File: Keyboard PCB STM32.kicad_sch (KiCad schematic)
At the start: 18 parts, among them J1 USB_C_Receptacle_USB2.0_14P, SW68 SW_Push, U1 XC6206PxxxMR, U2 SRV05-4, U3 STM32F072CBTx

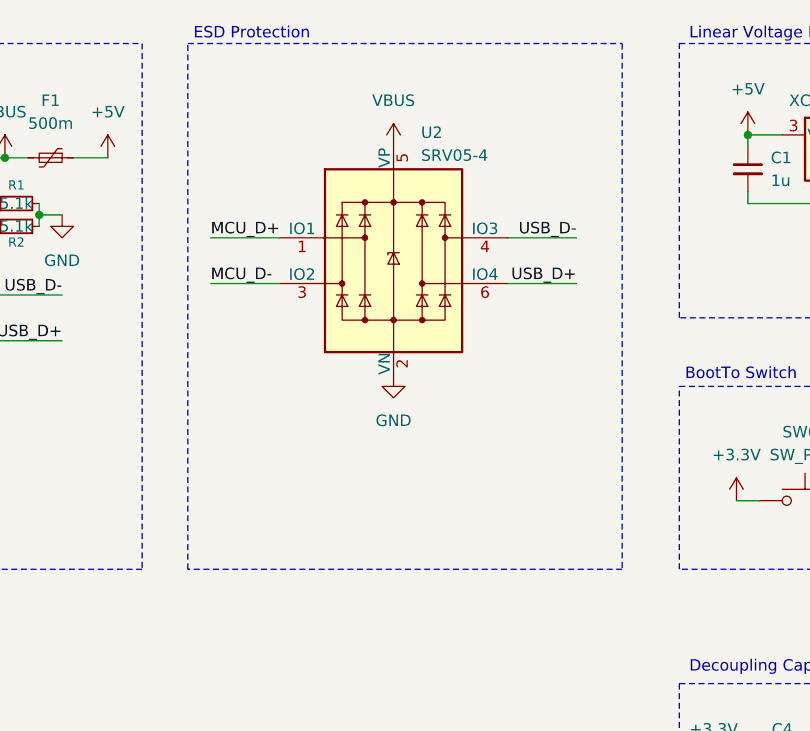
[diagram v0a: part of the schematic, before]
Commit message: Update to ESD protection
Changed ESD from SRV05-4 to USBLC6-2SC6
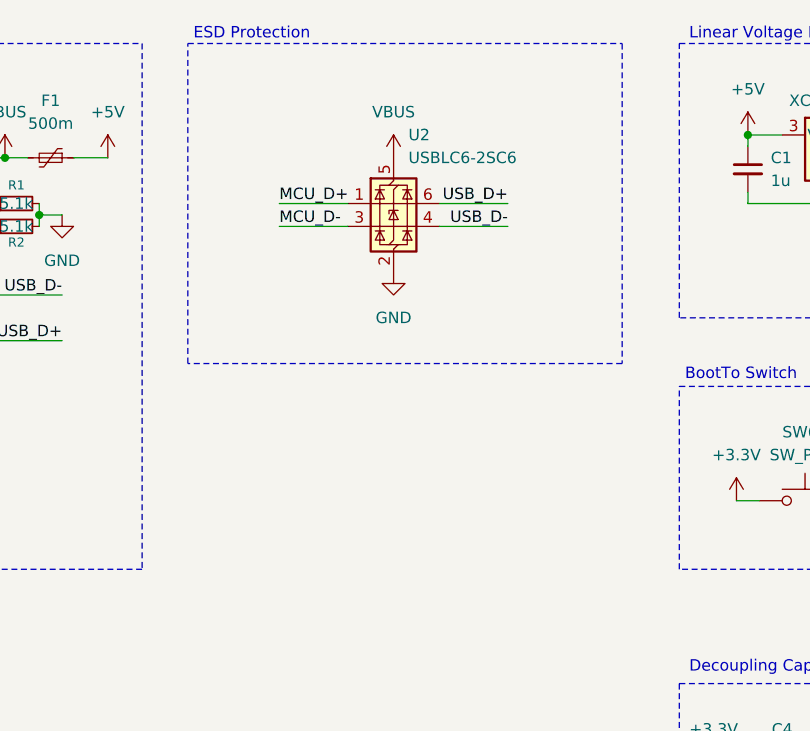
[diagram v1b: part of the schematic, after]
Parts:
- removed U2: SRV05-4, Package_TO_SOT_SMD:SOT-23-6, symbol Power_Protection:SRV05-4
- added U2: USBLC6-2SC6, Package_TO_SOT_SMD:SOT-23-6, symbol Power_Protection:USBLC6-2SC6
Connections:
- net GND: now also U2.2 (GND)
- net MCU_D+: now also U2.1 (I/O1)
- net MCU_D-: now also U2.3 (I/O2)
- net USB_D+: now also U2.6 (I/O1)
- net USB_D-: now also U2.4 (I/O2)
- net VBUS: now also U2.5 (VBUS)
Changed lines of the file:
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@@
 	(rectangle
 		(start 78.74 27.94)
-		(end 127 86.36)
+		(end 127 63.5)
 		(stroke
 			(width 0)
@@
 	(wire
 		(pts
-			(xy 81.28 49.53) (xy 88.9 49.53)
+			(xy 54.61 55.88) (xy 55.88 55.88)
 		)
 		(stroke
@@
 	(wire
 		(pts
-			(xy 54.61 55.88) (xy 55.88 55.88)
+			(xy 160.02 38.1) (xy 162.56 38.1)
 		)
 		(stroke
@@
 	(wire
 		(pts
-			(xy 160.02 38.1) (xy 162.56 38.1)
+			(xy 62.23 46.99) (xy 62.23 48.26)
 		)
 		(stroke
@@
 	(wire
 		(pts
-			(xy 62.23 46.99) (xy 62.23 48.26)
+			(xy 140.97 38.1) (xy 140.97 39.37)
 		)
 		(stroke
@@
 	(wire
 		(pts
-			(xy 140.97 38.1) (xy 140.97 39.37)
+			(xy 162.56 38.1) (xy 162.56 39.37)
 		)
 		(stroke
@@
 	(wire
 		(pts
-			(xy 162.56 38.1) (xy 162.56 39.37)
+			(xy 217.17 38.1) (xy 219.71 38.1)
 		)
 		(stroke
@@
 	(wire
 		(pts
-			(xy 217.17 38.1) (xy 219.71 38.1)
+			(xy 88.9 48.26) (xy 96.52 48.26)
 		)
 		(stroke
@@
 	(wire
 		(pts
-			(xy 114.3 49.53) (xy 121.92 49.53)
+			(xy 165.1 78.74) (xy 167.64 78.74)
 		)
 		(stroke
@@
 	(wire
 		(pts
-			(xy 81.28 54.61) (xy 88.9 54.61)
+			(xy 162.56 45.72) (xy 162.56 44.45)
 		)
 		(stroke
@@
 	(wire
 		(pts
-			(xy 165.1 78.74) (xy 167.64 78.74)
+			(xy 154.94 109.22) (xy 149.86 109.22)
 		)
 		(stroke
@@
 	(wire
 		(pts
-			(xy 162.56 45.72) (xy 162.56 44.45)
+			(xy 152.4 78.74) (xy 157.48 78.74)
 		)
 		(stroke
@@
 	(wire
 		(pts
-			(xy 154.94 109.22) (xy 149.86 109.22)
+			(xy 31.75 78.74) (xy 39.37 78.74)
 		)
 		(stroke
@@
 	(wire
 		(pts
-			(xy 152.4 78.74) (xy 157.48 78.74)
+			(xy 55.88 53.34) (xy 55.88 55.88)
 		)
 		(stroke
@@
 	(wire
 		(pts
-			(xy 31.75 78.74) (xy 39.37 78.74)
+			(xy 88.9 45.72) (xy 96.52 45.72)
 		)
 		(stroke
@@
 	(wire
 		(pts
-			(xy 55.88 53.34) (xy 55.88 55.88)
+			(xy 62.23 46.99) (xy 64.77 46.99)
 		)
 		(stroke
@@
 	(wire
 		(pts
-			(xy 62.23 46.99) (xy 64.77 46.99)
+			(xy 66.04 40.64) (xy 69.85 40.64)
 		)
 		(stroke
@@
 	(wire
 		(pts
-			(xy 114.3 54.61) (xy 121.92 54.61)
+			(xy 106.68 48.26) (xy 114.3 48.26)
 		)
 		(stroke
@@
 	(wire
 		(pts
-			(xy 66.04 40.64) (xy 69.85 40.64)
+			(xy 165.1 109.22) (xy 170.18 109.22)
 		)
 		(stroke
@@
 	(wire
 		(pts
-			(xy 165.1 109.22) (xy 170.18 109.22)
+			(xy 154.94 114.3) (xy 160.02 114.3)
 		)
 		(stroke
@@
 	(wire
 		(pts
-			(xy 154.94 114.3) (xy 160.02 114.3)
+			(xy 64.77 55.88) (xy 55.88 55.88)
 		)
 		(stroke
@@
 	(wire
 		(pts
-			(xy 64.77 55.88) (xy 55.88 55.88)
+			(xy 106.68 45.72) (xy 114.3 45.72)
 		)
 		(stroke
@@
 	)
 	(label "USB_D+"
-		(at 121.92 54.61 180)
+		(at 114.3 45.72 180)
 		(effects
 			(font
@@
 	)
 	(label "MCU_D-"
-		(at 81.28 54.61 0)
+		(at 88.9 48.26 0)
 		(effects
 			(font
@@
 	)
 	(label "USB_D-"
-		(at 121.92 49.53 180)
+		(at 114.3 48.26 180)
 		(effects
 			(font
@@
 	)
 	(label "MCU_D+"
-		(at 81.28 49.53 0)
+		(at 88.9 45.72 0)
 		(effects
 			(font
@@
 	(symbol
 		(lib_id "power:GND")
-		(at 101.6 64.77 0)
+		(at 101.6 53.34 0)
 		(unit 1)
 		(exclude_from_sim no)
@@
 		(fields_autoplaced yes)
 		(property "Reference" "#PWR06"
-			(at 101.6 71.12 0)
+			(at 101.6 59.69 0)
 			(effects
 				(font
@@
 		)
 		(property "Value" "GND"
-			(at 101.6 69.85 0)
+			(at 101.6 58.42 0)
 			(effects
 				(font
@@
 		)
 		(property "Footprint" ""
-			(at 101.6 64.77 0)
+			(at 101.6 53.34 0)
 			(effects
 				(font
@@
 		)
 		(property "Datasheet" ""
-			(at 101.6 64.77 0)
+			(at 101.6 53.34 0)
 			(effects
 				(font
@@
 		)
 		(property "Description" "Power symbol creates a global label with name \"GND\" , ground"
-			(at 101.6 64.77 0)
+			(at 101.6 53.34 0)
 			(effects
 				(font
@@
 		)
 		(instances
-			(project ""
+			(project "Keyboard PCB STM32"
 				(path "/d7b46417-6e9b-40e7-895f-68f7a27257b4"
 					(reference "#PWR06")
@@
 	)
 	(symbol
+		(lib_id "Power_Protection:USBLC6-2SC6")
+		(at 101.6 45.72 0)
+		(unit 1)
+		(exclude_from_sim no)
+		(in_bom yes)
+		(on_board yes)
+		(dnp no)
+		(fields_autoplaced yes)
+		(property "Reference" "U2"
+			(at 103.2511 38.1 0)
+			(effects
+				(font
+					(size 1.27 1.27)
+				)
+				(justify left)
+			)
+		)
+		(property "Value" "USBLC6-2SC6"
+			(at 103.2511 40.64 0)
+			(effects
+				(font
+					(size 1.27 1.27)
+				)
+				(justify left)
+			)
+		)
+		(property "Footprint" "Package_TO_SOT_SMD:SOT-23-6"
+			(at 102.87 52.07 0)
+			(effects
+				(font
+					(size 1.27 1.27)
+					(italic yes)
+				)
+				(justify left)
+				(hide yes)
+			)
+		)
+		(property "Datasheet" "https://www.st.com/resource/en/datasheet/usblc6-2.pdf"
+			(at 102.87 53.975 0)
+			(effects
+				(font
+					(size 1.27 1.27)
+				)
+				(justify left)
+				(hide yes)
+			)
+		)
+		(property "Description" "Very low capacitance ESD protection diode, 2 data-line, SOT-23-6"
+			(at 101.6 45.72 0)
+			(effects
+				(font
+					(size 1.27 1.27)
+				)
+				(hide yes)
+			)
+		)
+		(pin "4"
+		)
+		(pin "1"
+		)
+		(pin "2"
+		)
+		(pin "6"
+		)
+		(pin "3"
+		)
+		(pin "5"
+		)
+		(instances
+			(project ""
+				(path "/d7b46417-6e9b-40e7-895f-68f7a27257b4"
+					(reference "U2")
+					(unit 1)
+				)
+			)
+		)
+	)
+	(symbol
 		(lib_id "Device:C_Small")
 		(at 140.97 41.91 0)
@@
 	(symbol
 		(lib_id "power:VBUS")
-		(at 101.6 39.37 0)
+		(at 101.6 40.64 0)
 		(unit 1)
 		(exclude_from_sim no)
@@
 		(fields_autoplaced yes)
 		(property "Reference" "#PWR013"
-			(at 101.6 43.18 0)
+			(at 101.6 44.45 0)
 			(effects
 				(font
@@
 		)
 		(property "Value" "VBUS"
-			(at 101.6 34.29 0)
+			(at 101.6 35.56 0)
 			(effects
 				(font
@@
 		)
 		(property "Footprint" ""
-			(at 101.6 39.37 0)
+			(at 101.6 40.64 0)
 			(effects
 				(font
@@
 		)
 		(property "Datasheet" ""
-			(at 101.6 39.37 0)
+			(at 101.6 40.64 0)
 			(effects
 				(font
@@
 		)
 		(property "Description" "Power symbol creates a global label with name \"VBUS\""
-			(at 101.6 39.37 0)
+			(at 101.6 40.64 0)
 			(effects
 				(font
@@
 		)
 		(instances
-			(project ""
+			(project "Keyboard PCB STM32"
 				(path "/d7b46417-6e9b-40e7-895f-68f7a27257b4"
 					(reference "#PWR013")
@@
 					(unit 1)
 				)
-			)
-		)
-	)
-	(symbol
-		(lib_id "Power_Protection:SRV05-4")
-		(at 101.6 52.07 0)
-		(unit 1)
-		(exclude_from_sim no)
-		(in_bom yes)
-		(on_board yes)
-		(dnp no)
-		(property "Reference" "U2"
-			(at 104.648 37.846 0)
-			(effects
-				(font
-					(size 1.27 1.27)
-				)
-				(justify left)
-			)
-		)
-		(property "Value" "SRV05-4"
-			(at 104.648 40.386 0)
-			(effects
-				(font
-					(size 1.27 1.27)
-				)
-				(justify left)
-			)
-		)
-		(property "Footprint" "Package_TO_SOT_SMD:SOT-23-6"
-			(at 119.38 63.5 0)
-			(effects
-				(font
-					(size 1.27 1.27)
-				)
-				(hide yes)
-			)
-		)
-		(property "Datasheet" "http://www.onsemi.com/pub/Collateral/SRV05-4-D.PDF"
-			(at 101.6 52.07 0)
-			(effects
-				(font
-					(size 1.27 1.27)
-				)
-				(hide yes)
-			)
-		)
-		(property "Description" "ESD Protection Diodes with Low Clamping Voltage, SOT-23-6"
-			(at 101.6 52.07 0)
-			(effects
-				(font
-					(size 1.27 1.27)
-				)
-				(hide yes)
-			)
-		)
-		(pin "2"
-		)
-		(pin "6"
-		)
-		(pin "1"
-		)
-		(pin "4"
-		)
-		(pin "3"
-		)
-		(pin "5"
-		)
-		(instances
-			(project ""
-				(path "/d7b46417-6e9b-40e7-895f-68f7a27257b4"
-					(reference "U2")
-					(unit 1)
-				)

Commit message: Add files via upload
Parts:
- added SW69: SW_Push, Button_Switch_SMD:SW_Push_1P1T_XKB_TS-1187A, symbol Switch:SW_Push
- SW68: footprint Button_Switch_SMD:SW_SPST_TS-1088-xR020 -> Button_Switch_SMD:Panasonic_EVQPUL_EVQPUC
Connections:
- net +3.3V: now also SW69.1
- net BOOT: now also SW69.2
- no-connect marks 14 -> 15
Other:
- moved on the sheet: R3, SW68
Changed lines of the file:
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@@
 	)
 	(rectangle
-		(start 133.35 66.04)
-		(end 172.72 86.36)
+		(start 133.35 63.5)
+		(end 172.72 90.17)
 		(stroke
 			(width 0)
@@
 	(text "BootTo Switch"
 		(exclude_from_sim no)
-		(at 140.208 64.77 0)
+		(at 140.208 62.23 0)
 		(effects
 			(font
@@
 	)
 	(junction
+		(at 152.4 73.66)
+		(diameter 0)
+		(color 0 0 0 0)
+	)
+	(junction
 		(at 219.71 38.1)
 		(diameter 0)
@@
 	)
 	(junction
+		(at 142.24 73.66)
+		(diameter 0)
+		(color 0 0 0 0)
+	)
+	(junction
 		(at 154.94 109.22)
 		(diameter 0)
@@
 	)
 	(no_connect
+		(at 240.03 50.8)
+	)
+	(no_connect
 		(at 204.47 96.52)
 	)
@@
 	(wire
 		(pts
+			(xy 152.4 73.66) (xy 152.4 85.09)
+		)
+		(stroke
+			(width 0)
+			(type default)
+		)
+	)
+	(wire
+		(pts
 			(xy 54.61 55.88) (xy 55.88 55.88)
 		)
@@
 	(wire
 		(pts
+			(xy 142.24 73.66) (xy 142.24 85.09)
+		)
+		(stroke
+			(width 0)
+			(type default)
+		)
+	)
+	(wire
+		(pts
 			(xy 88.9 48.26) (xy 96.52 48.26)
 		)
@@
 	(wire
 		(pts
-			(xy 165.1 78.74) (xy 167.64 78.74)
+			(xy 162.56 45.72) (xy 162.56 44.45)
 		)
 		(stroke
@@
 	(wire
 		(pts
-			(xy 162.56 45.72) (xy 162.56 44.45)
+			(xy 154.94 109.22) (xy 149.86 109.22)
 		)
 		(stroke
@@
 	(wire
 		(pts
-			(xy 154.94 109.22) (xy 149.86 109.22)
+			(xy 152.4 73.66) (xy 157.48 73.66)
 		)
 		(stroke
@@
 	(wire
 		(pts
-			(xy 152.4 78.74) (xy 157.48 78.74)
+			(xy 31.75 78.74) (xy 39.37 78.74)
 		)
 		(stroke
@@
 	(wire
 		(pts
-			(xy 31.75 78.74) (xy 39.37 78.74)
+			(xy 167.64 73.66) (xy 165.1 73.66)
 		)
 		(stroke
@@
 	(wire
 		(pts
-			(xy 139.7 78.74) (xy 142.24 78.74)
+			(xy 139.7 73.66) (xy 142.24 73.66)
 		)
 		(stroke
@@
 		)
 	)
-	(global_label "BOOT"
-		(shape input)
-		(at 154.94 78.74 90)
-		(fields_autoplaced yes)
-		(effects
-			(font
-				(size 1.27 1.27)
-			)
-			(justify left)
-		)
-		(property "Intersheetrefs" "${INTERSHEET_REFS}"
-			(at 154.94 70.8562 90)
-			(effects
-				(font
-					(size 1.27 1.27)
-				)
-				(justify left)
-				(hide yes)
-			)
-		)
-	)
 	(global_label "R1"
 		(shape input)
@@
 		)
 	)
+	(global_label "BOOT"
+		(shape input)
+		(at 154.94 73.66 90)
+		(fields_autoplaced yes)
+		(effects
+			(font
+				(size 1.27 1.27)
+			)
+			(justify left)
+		)
+		(property "Intersheetrefs" "${INTERSHEET_REFS}"
+			(at 154.94 65.7762 90)
+			(effects
+				(font
+					(size 1.27 1.27)
+				)
+				(justify left)
+				(hide yes)
+			)
+		)
+	)
 	(global_label "R3"
 		(shape input)
@@
 	(symbol
 		(lib_id "power:GND")
-		(at 167.64 78.74 0)
+		(at 167.64 73.66 0)
 		(unit 1)
 		(exclude_from_sim no)
@@
 		(fields_autoplaced yes)
 		(property "Reference" "#PWR05"
-			(at 167.64 85.09 0)
+			(at 167.64 80.01 0)
 			(effects
 				(font
@@
 		)
 		(property "Value" "GND"
-			(at 167.64 83.82 0)
+			(at 167.64 78.74 0)
 			(effects
 				(font
@@
 		)
 		(property "Footprint" ""
-			(at 167.64 78.74 0)
+			(at 167.64 73.66 0)
 			(effects
 				(font
@@
 		)
 		(property "Datasheet" ""
-			(at 167.64 78.74 0)
+			(at 167.64 73.66 0)
 			(effects
 				(font
@@
 		)
 		(property "Description" "Power symbol creates a global label with name \"GND\" , ground"
-			(at 167.64 78.74 0)
+			(at 167.64 73.66 0)
 			(effects
 				(font
@@
 	(symbol
 		(lib_id "Device:R")
-		(at 161.29 78.74 90)
+		(at 161.29 73.66 90)
 		(unit 1)
 		(exclude_from_sim no)
@@
 		(dnp no)
 		(property "Reference" "R3"
-			(at 161.29 73.914 90)
+			(at 161.29 68.834 90)
 			(effects
 				(font
@@
 		)
 		(property "Value" "10k"
-			(at 161.29 76.454 90)
+			(at 161.29 71.374 90)
 			(effects
 				(font
@@
 		)
 		(property "Footprint" "Resistor_SMD:R_0805_2012Metric"
-			(at 161.29 80.518 90)
+			(at 161.29 75.438 90)
 			(effects
 				(font
@@
 		)
 		(property "Datasheet" "~"
-			(at 161.29 78.74 0)
+			(at 161.29 73.66 0)
 			(effects
 				(font
@@
 		)
 		(property "Description" "Resistor"
-			(at 161.29 78.74 0)
+			(at 161.29 73.66 0)
 			(effects
 				(font
@@
 	)
 	(symbol
+		(lib_id "Switch:SW_Push")
+		(at 147.32 85.09 0)
+		(unit 1)
+		(exclude_from_sim no)
+		(in_bom yes)
+		(on_board yes)
+		(dnp no)
+		(fields_autoplaced yes)
+		(property "Reference" "SW69"
+			(at 147.32 77.47 0)
+			(effects
+				(font
+					(size 1.27 1.27)
+				)
+			)
+		)
+		(property "Value" "SW_Push"
+			(at 147.32 80.01 0)
+			(effects
+				(font
+					(size 1.27 1.27)
+				)
+			)
+		)
+		(property "Footprint" "Button_Switch_SMD:SW_Push_1P1T_XKB_TS-1187A"
+			(at 147.32 80.01 0)
+			(effects
+				(font
+					(size 1.27 1.27)
+				)
+				(hide yes)
+			)
+		)
+		(property "Datasheet" "~"
+			(at 147.32 80.01 0)
+			(effects
+				(font
+					(size 1.27 1.27)
+				)
+				(hide yes)
+			)
+		)
+		(property "Description" "Push button switch, generic, two pins"
+			(at 147.32 85.09 0)
+			(effects
+				(font
+					(size 1.27 1.27)
+				)
+				(hide yes)
+			)
+		)
+		(pin "2"
+		)
+		(pin "1"
+		)
+		(instances
+			(project ""
+				(path "/d7b46417-6e9b-40e7-895f-68f7a27257b4"
+					(reference "SW69")
+					(unit 1)
+				)
+			)
+		)
+	)
+	(symbol
 		(lib_id "power:PWR_FLAG")
 		(at 142.24 144.78 180)
@@
 	(symbol
 		(lib_id "power:+3.3V")
-		(at 139.7 78.74 0)
+		(at 139.7 73.66 0)
 		(unit 1)
 		(exclude_from_sim no)
@@
 		(fields_autoplaced yes)
 		(property "Reference" "#PWR04"
-			(at 139.7 82.55 0)
+			(at 139.7 77.47 0)
 			(effects
 				(font
@@
 		)
 		(property "Value" "+3.3V"
-			(at 139.7 73.66 0)
+			(at 139.7 68.58 0)
 			(effects
 				(font
@@
 		)
 		(property "Footprint" ""
-			(at 139.7 78.74 0)
+			(at 139.7 73.66 0)
 			(effects
 				(font
@@
 		)
 		(property "Datasheet" ""
-			(at 139.7 78.74 0)
+			(at 139.7 73.66 0)
 			(effects
 				(font
@@
 		)
 		(property "Description" "Power symbol creates a global label with name \"+3.3V\""
-			(at 139.7 78.74 0)
+			(at 139.7 73.66 0)
 			(effects
 				(font
@@
 	(symbol
 		(lib_id "Switch:SW_Push")
-		(at 147.32 78.74 0)
+		(at 147.32 73.66 0)
 		(unit 1)
 		(exclude_from_sim no)
@@
 		(fields_autoplaced yes)
 		(property "Reference" "SW68"
-			(at 147.32 71.12 0)
+			(at 147.32 66.04 0)
 			(effects
 				(font
@@
 		)
 		(property "Value" "SW_Push"
-			(at 147.32 73.66 0)
+			(at 147.32 68.58 0)
 			(effects
 				(font
@@
 			)
 		)
-		(property "Footprint" "Button_Switch_SMD:SW_SPST_TS-1088-xR020"
-			(at 147.32 73.66 0)
+		(property "Footprint" "Button_Switch_SMD:Panasonic_EVQPUL_EVQPUC"
+			(at 147.32 68.58 0)
 			(effects
 				(font
@@
 		)
 		(property "Datasheet" "~"
-			(at 147.32 73.66 0)
+			(at 147.32 68.58 0)
 			(effects
 				(font
@@
 		)
 		(property "Description" "Push button switch, generic, two pins"
-			(at 147.32 78.74 0)
+			(at 147.32 73.66 0)
 			(effects
 				(font
